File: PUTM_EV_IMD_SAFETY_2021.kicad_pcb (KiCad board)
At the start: 2 copper layers, 70 x 55 mm, 54 parts, among them J1 Conn_01x06, J2 Conn_01x02, K1 FINDER-30.22.7.005.0010, Q1 2N7002, U1 SN74LS32D, U10 74LVC1G79, U11 74LVC1G79, U2 MC78M12CDTG, U3 LM1117IMP-5.0, U4 LM393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

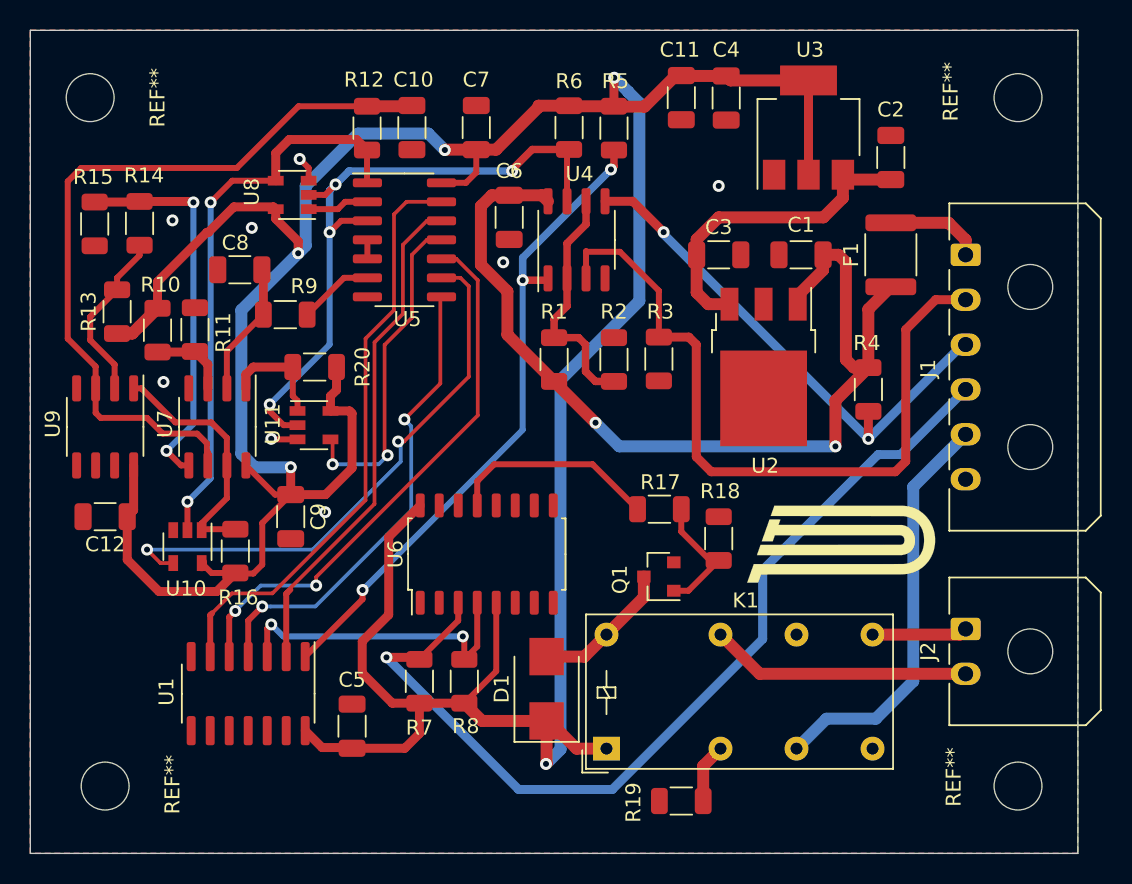
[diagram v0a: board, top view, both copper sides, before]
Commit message: PCB Routed and signed with v2 version
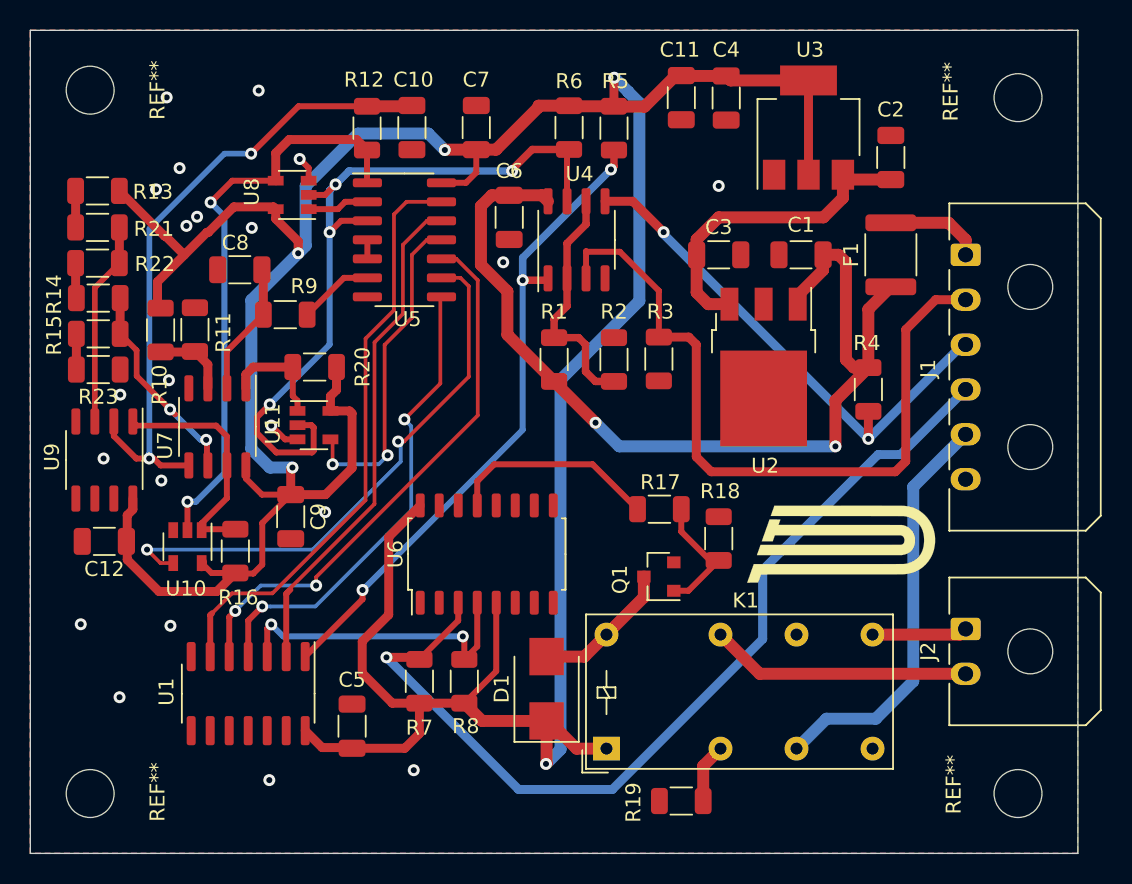
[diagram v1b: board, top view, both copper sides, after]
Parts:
- added G***: LOGO, Logos:PUTM_LOGO_22mm, B.Cu at (144.6, 106.8)
- added G***: LOGO, Logos:SignatureBox37mm, B.Cu at (165.3, 87.0)
- added R21: 0k, Resistor_SMD:R_1206_3216Metric, F.Cu at (129.5, 80.7)
- added R22: 0k, Resistor_SMD:R_1206_3216Metric, F.Cu at (129.5, 83.1)
- added R23: 0k, Resistor_SMD:R_1206_3216Metric, F.Cu at (129.5, 90.2)
- moved R13 8.17 mm to (129.5, 78.2), turned to 0 degrees
- moved R15 7.35 mm to (129.5, 87.8), turned to 0 degrees
- moved R14 5.71 mm to (129.5, 85.4), turned to 180 degrees
- moved U9 2.22 mm to (129.9, 96.2)
- moved C12 1.65 mm to (129.9, 101.7)
- moved REF** 1.12 mm to (129.0, 118.5)
- moved REF** 0.50 mm to (129.0, 71.5)
- moved REF** 0.50 mm to (191.0, 118.5)
- moved R10 0.21 mm to (133.7, 87.5)
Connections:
- R14 pad 2: Net-(R13-Pad1) -> Net-(R14-Pad2)
- R15 pad 1: GND -> Net-(R15-Pad1)
- U7 pad 5: Net-(R14-Pad1) -> Net-(C10-Pad1)
- U7 pad 6: Net-(C10-Pad1) -> Net-(R14-Pad1)
- U9 pad 2: Net-(R13-Pad1) -> Net-(C10-Pad1)
- U9 pad 3: Net-(C10-Pad1) -> Net-(R21-Pad1)
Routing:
- net Net-(R21-Pad1): track 0.00 -> 13.6 mm
- net Net-(R14-Pad1): track 25.9 -> 14.3 mm
- net Net-(R13-Pad1): track 11.6 -> 2.44 mm
- net Net-(C10-Pad1): track 51.1 -> 43.1 mm, vias 0 -> 2
- net PWM_TTL: track 44.3 -> 50.9 mm
- net Net-(R15-Pad1): track 0.00 -> 2.39 mm
- net Net-(R14-Pad2): track 0.00 -> 2.36 mm
- net Net-(R12-Pad2): track 38.3 -> 39.4 mm
- net Net-(R16-Pad2): track 16.7 -> 15.9 mm
- net GND: track 3.47 -> 3.84 mm, vias 8 -> 21
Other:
- board text added: "Tomasz Wojciechowski Szymon Sambor IMDSafety_2022_V2"

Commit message: Project converted to Kicad6, Schematic beatuyfing
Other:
- net class Default removed
